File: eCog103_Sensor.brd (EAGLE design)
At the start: 48 x 28 mm, 1 part

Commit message: V1.1
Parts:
- added U$1: SENSOR, eCogs:SENSOR-HJX4
- ECOG: value ECOG_BUSES_ROWECOG_BUSES_SMD -> ECOG_GENERAL_ROWECOG_GENERAL_SMD; device eCogs:ECOG_BUSES_SMD -> eCogs:ECOG_GENERAL_SMD
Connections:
- new net A1: ECOG.1, U$1.DO/S
- new net A2: ECOG.2, U$1.AO
- new net A3: ECOG.3
- net 3V3: now also U$1.+
- net GND: now also U$1.GND
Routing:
- net A2: track 0.00 -> 51.8 mm
- net A1: track 0.00 -> 43.7 mm
- net 3V3: track 3.55 -> 7.06 mm
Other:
- board text added: "AO"
- board text added: "Cut Out"
- board text added: "DO/S"
- board text added: "Sensor"
- board text added: "ecog103 v1.0"
- board text added: "ecog103.GadgetFactory.net"
- board text removed: "I2C-SCL"
- board text removed: "I2C-SDA"
- board text removed: "P5<>"
- board text removed: "Project Name"
- board text removed: "RESET"
- board text removed: "SPI-CS>"
- board text removed: "SPI-MOSI<"
- board text removed: "SPI-MOSI>"
- board text removed: "SPI-SCK>"
- board text removed: "ecog100 v1.0"
- board text removed: "ecog100.GadgetFactory.net"

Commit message: Latest updated to V1.4
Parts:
- added U$2, U$3: (no value), eCogs:LEGEND_ANALOG
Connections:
- removed net A3: ECOG.3
- net A1: now also ECOG.G0, U$1.AO; no longer ECOG.1, U$1.DO/S
- net A2: now also ECOG.G1, U$1.DO/S; no longer ECOG.2, U$1.AO
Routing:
- net A2: track 51.8 -> 42.2 mm
- net A1: track 43.7 -> 52.4 mm
- net 3V3: track 7.06 -> 4.80 mm
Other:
- outline, holes or cut-outs redrawn
- board text added: "ecog103 v1.1"
- board text removed: "5V"
- board text removed: "ecog103 v1.0"

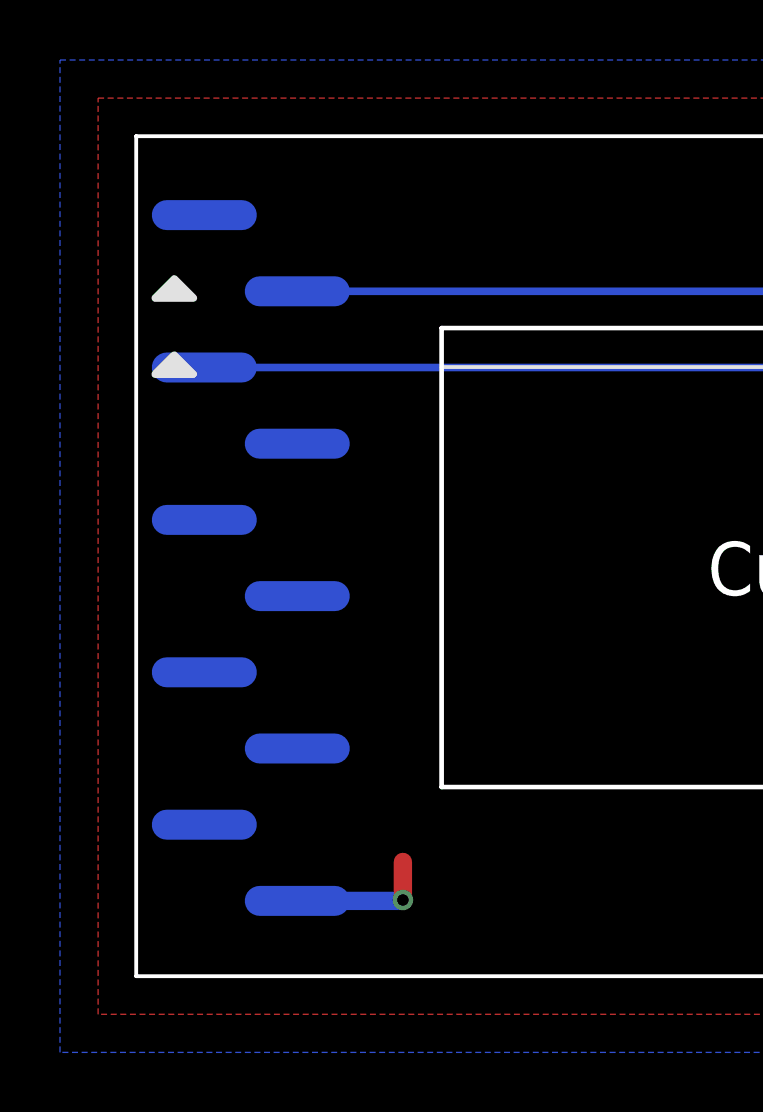
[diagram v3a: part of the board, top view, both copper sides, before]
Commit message: Added Box text to silkscreen
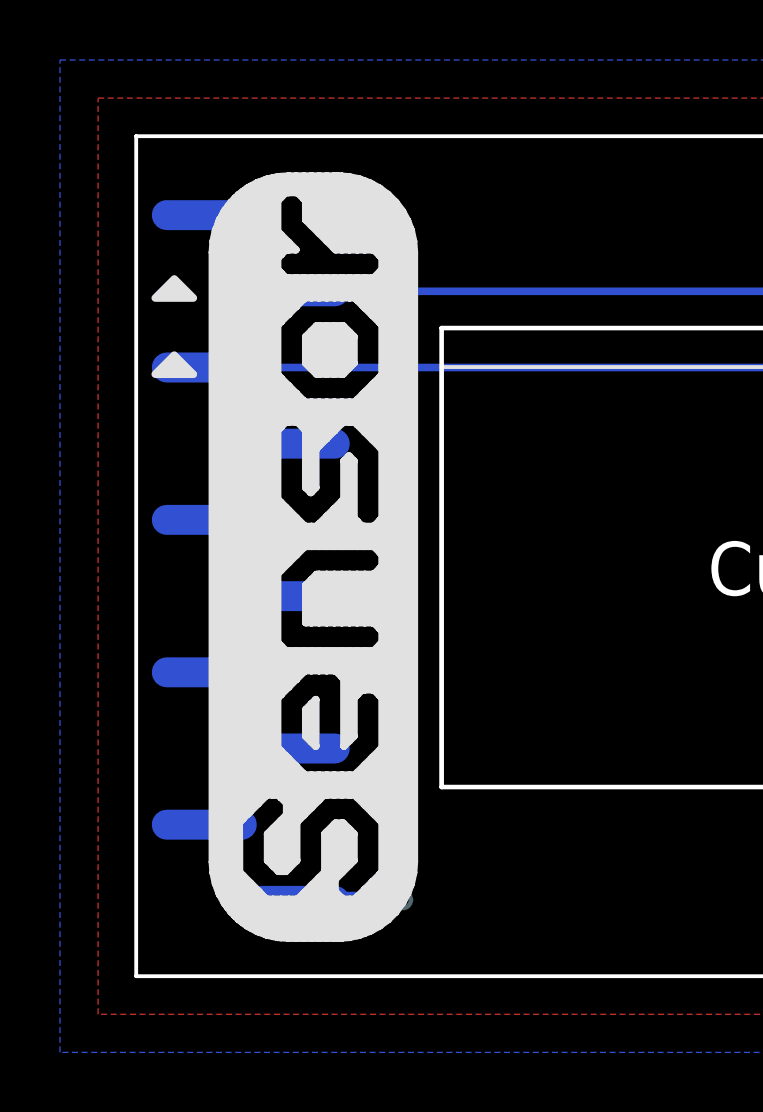
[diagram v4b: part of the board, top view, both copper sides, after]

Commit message: Update all of the Fonts and graphics
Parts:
- added U$4, U$6: (no value), GadgetFactory:GADGETBOX_SMALL
- added U$5: (no value), ohw-logo:OSHW_FILLX150_NOTEXT
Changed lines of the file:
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@@
 <element name="U$2" library="eCogs" package="LEGEND_ANALOG" value="" x="1.27" y="22.86"/>
 <element name="U$3" library="eCogs" package="LEGEND_ANALOG" value="" x="1.27" y="20.32"/>
+<element name="U$4" library="GadgetFactory" package="GADGETBOX_SMALL" value="" x="23.495" y="25.019"/>
+<element name="U$5" library="ohw-logo" package="OSHW_FILLX150_NOTEXT" value="" x="36.83" y="22.86"/>
+<element name="U$6" library="GadgetFactory" package="GADGETBOX_SMALL" value="" x="28.575" y="2.921" rot="R180"/>
 </elements>
 <signals>

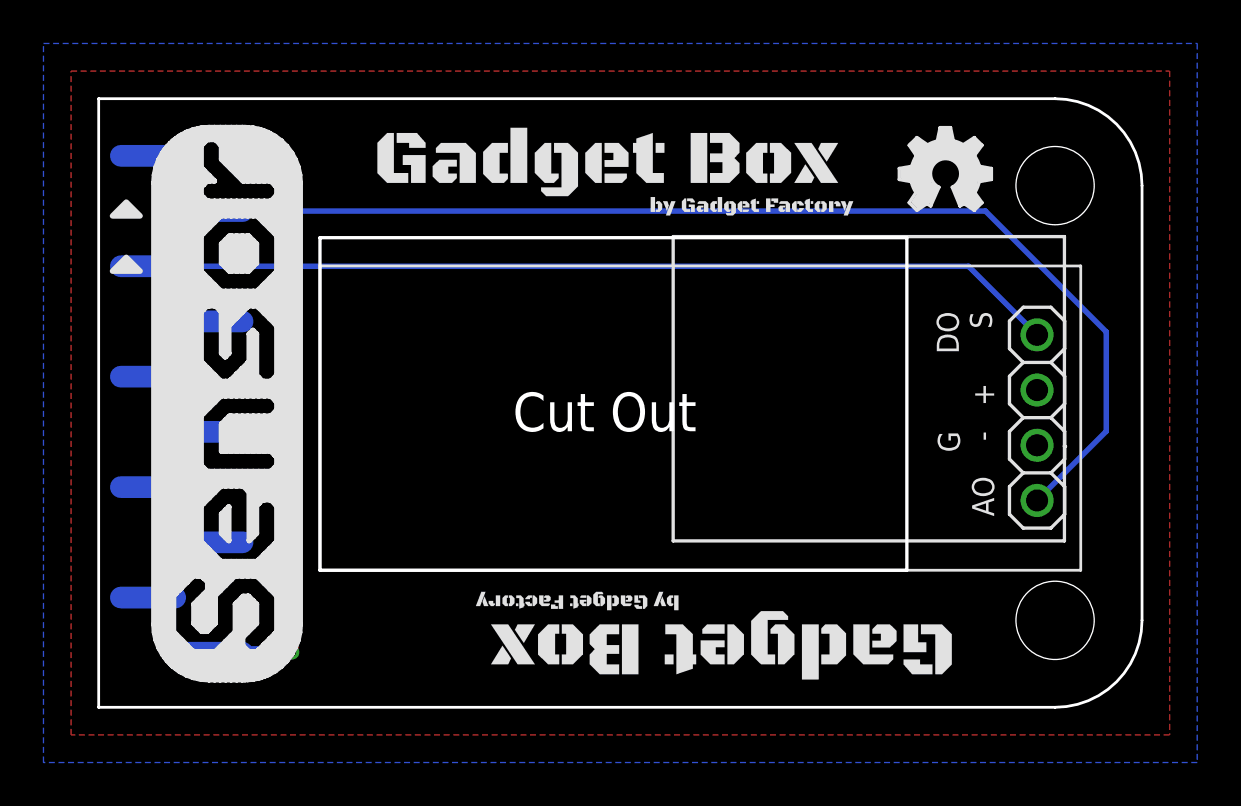
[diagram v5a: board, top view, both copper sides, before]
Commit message: Fix a trace on the Sensor eCog that went through cutout.
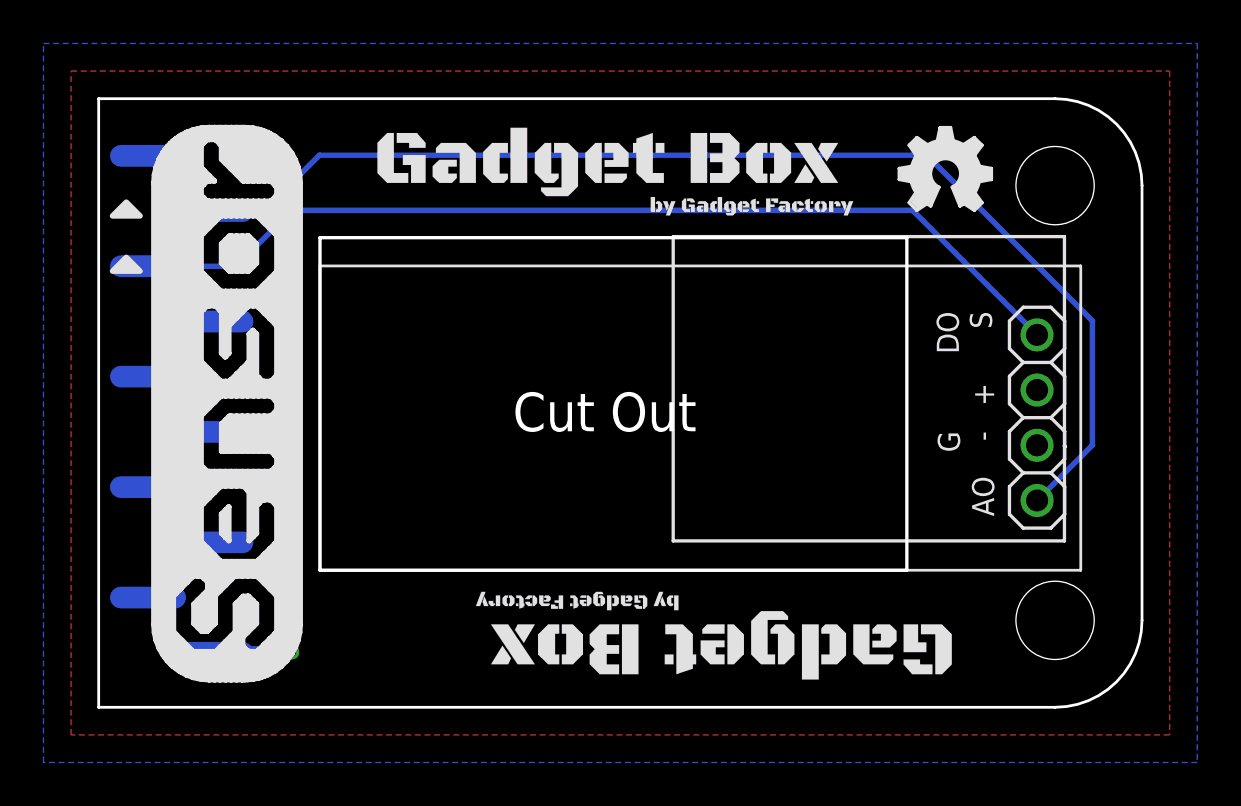
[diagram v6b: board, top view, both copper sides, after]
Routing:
- net A2: track 42.2 -> 44.3 mm
- net A1: track 52.4 -> 53.9 mm
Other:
- board text added: "ecog103 v1.2"
- board text removed: "ecog103 v1.1"
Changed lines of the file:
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@@
 <layer number="19" name="Unrouted" color="6" fill="1" visible="yes" active="yes"/>
 <layer number="20" name="Dimension" color="15" fill="1" visible="yes" active="yes"/>
-<layer number="21" name="tPlace" color="16" fill="1" visible="yes" active="yes"/>
+<layer number="21" name="tPlace" color="16" fill="1" visible="no" active="yes"/>
 <layer number="22" name="bPlace" color="14" fill="1" visible="yes" active="yes"/>
 <layer number="23" name="tOrigins" color="15" fill="1" visible="yes" active="yes"/>
@@
 <plain>
 <text x="31.529" y="26.415" size="0.8128" layer="22" font="vector" rot="MR0">ecog103.GadgetFactory.net</text>
-<text x="39.672" y="1.159" size="1.016" layer="22" font="vector" rot="MR0">ecog103 v1.1</text>
+<text x="39.672" y="1.159" size="1.016" layer="22" font="vector" rot="MR0">ecog103 v1.2</text>
 <text x="39.672" y="2.429" size="1.016" layer="22" font="vector" rot="MR0">Sensor</text>
 <text x="39.672" y="3.699" size="1.016" layer="22" font="vector" rot="MR0">eCogs</text>
@@
 <contactref element="U$1" pad="DO/S"/>
 <contactref element="ECOG" pad="G1"/>
-<wire x1="2.2706" y1="20.29" x2="40.016" y2="20.29" width="0.254" layer="16"/>
-<wire x1="40.016" y1="20.29" x2="43.171" y2="17.135" width="0.254" layer="16"/>
+<wire x1="2.2706" y1="20.29" x2="6.32" y2="20.29" width="0.254" layer="16"/>
+<wire x1="6.32" y1="20.29" x2="8.89" y2="22.86" width="0.254" layer="16"/>
+<wire x1="8.89" y1="22.86" x2="37.446" y2="22.86" width="0.254" layer="16"/>
+<wire x1="37.446" y1="22.86" x2="43.171" y2="17.135" width="0.254" layer="16"/>
 </signal>
 <signal name="A1">
 <contactref element="U$1" pad="AO"/>
 <contactref element="ECOG" pad="G0"/>
-<wire x1="5.3694" y1="22.83" x2="40.797" y2="22.83" width="0.254" layer="16"/>
-<wire x1="40.797" y1="22.83" x2="46.355" y2="17.272" width="0.254" layer="16"/>
-<wire x1="46.355" y1="17.272" x2="46.355" y2="12.699" width="0.254" layer="16"/>
-<wire x1="46.355" y1="12.699" x2="43.171" y2="9.515" width="0.254" layer="16"/>
+<wire x1="5.3694" y1="22.83" x2="7.59" y2="22.83" width="0.254" layer="16"/>
+<wire x1="7.59" y1="22.83" x2="10.16" y2="25.4" width="0.254" layer="16"/>
+<wire x1="10.16" y1="25.4" x2="38.1" y2="25.4" width="0.254" layer="16"/>
+<wire x1="38.1" y1="25.4" x2="45.72" y2="17.78" width="0.254" layer="16"/>
+<wire x1="45.72" y1="17.78" x2="45.72" y2="12.064" width="0.254" layer="16"/>
+<wire x1="45.72" y1="12.064" x2="43.171" y2="9.515" width="0.254" layer="16"/>
 </signal>
 </signals>

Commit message: All the 2.0 updates
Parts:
- moved U$2 48.2 mm to (47.0, 7.62)
- moved U$3 48.2 mm to (47.0, 5.08)
- moved U$5 5.08 mm to (41.9, 22.9)
- moved U$4 3.89 mm to (27.3, 24.3)
- moved U$1 1.02 mm to (46.2, 13.3)
- moved U$6 0.51 mm to (28.6, 3.43)
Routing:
- net 3V3: track 4.80 -> 46.1 mm, vias 1 -> 0
- net A1: track 53.9 -> 40.1 mm
- net A2: track 44.3 -> 41.7 mm
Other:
- board size 48 x 28 mm -> 47.5 x 28 mm
- board text added: "0"
- board text added: "1"
- board text added: "ecog103 v2.0"
- board text removed: "ecog103 v1.2"
